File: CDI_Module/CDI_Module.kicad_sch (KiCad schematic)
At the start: 0 parts

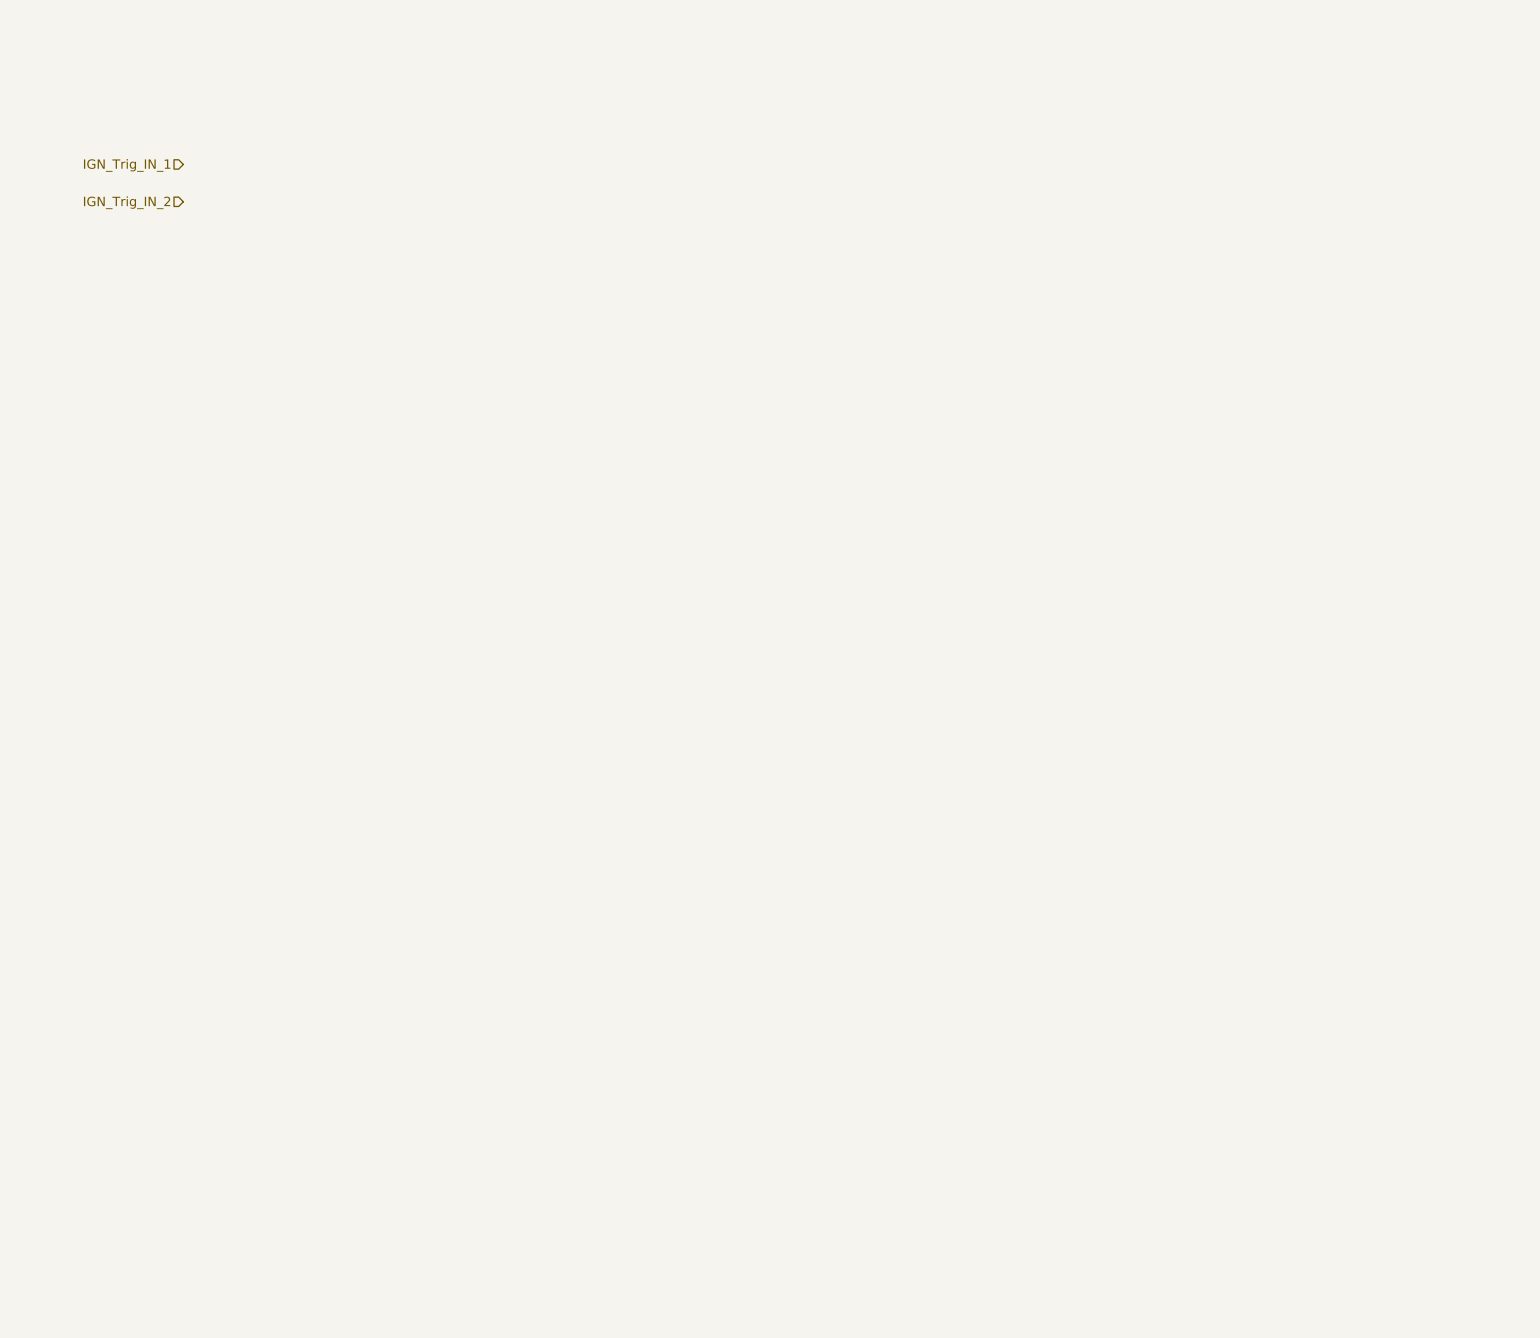
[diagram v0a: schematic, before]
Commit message: Updated security wiring and changed IGN driver for MOSFET
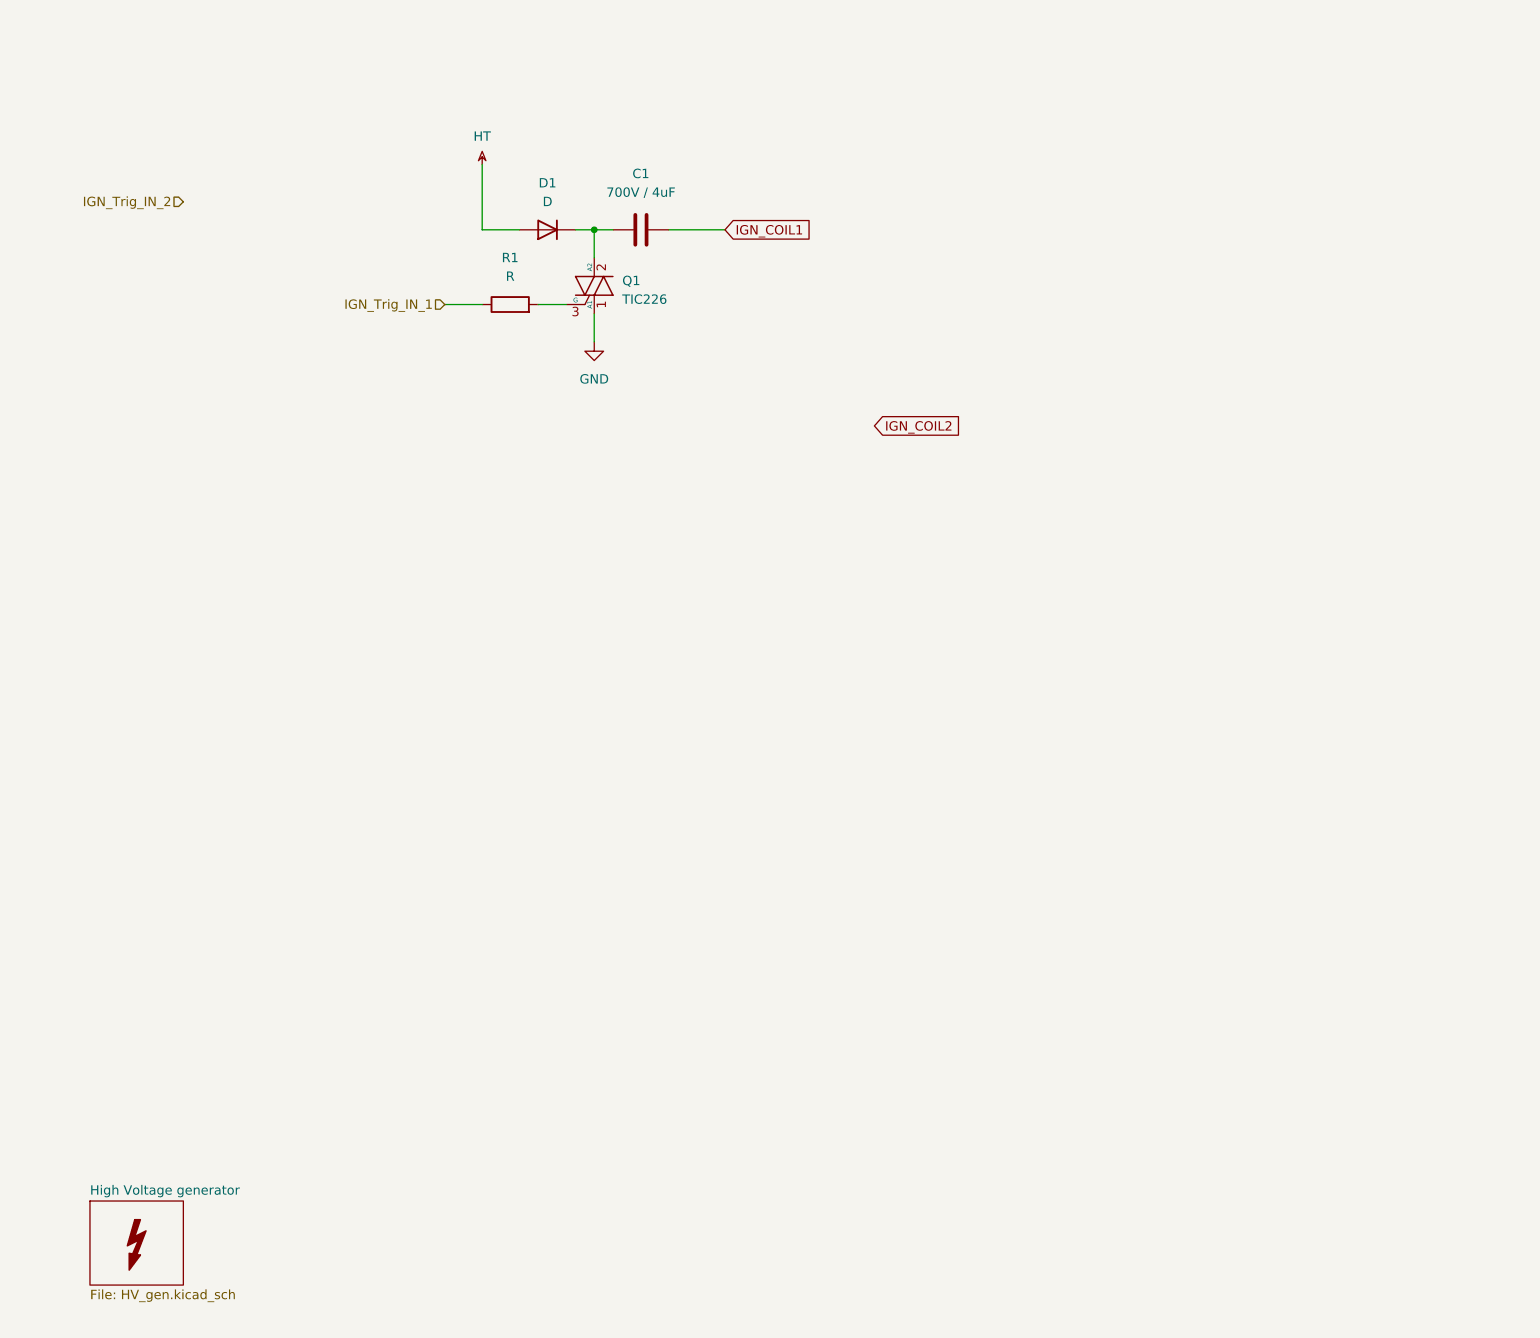
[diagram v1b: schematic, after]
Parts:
- added C1: 700V / 4uF, symbol Device:C
- added D1: D, Diode_SMD:D_0805_2012Metric_Pad1.15x1.40mm_HandSolder, symbol Device:D
- added Q1: TIC226, Package_TO_SOT_THT:TO-220-3_Vertical, symbol Triac_Thyristor:TIC226
- added R1: R, Resistor_SMD:R_0603_1608Metric_Pad0.98x0.95mm_HandSolder, symbol Device:R
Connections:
- net IGN_Trig_IN_1: now also R1.1
- new net: Q1.3 (G), R1.2
- new net: C1.1, D1.1 (K), Q1.2 (A2)
- new net GND: Q1.1 (A1)
- new net HT: D1.2 (A)
- new net IGN_COIL1: C1.2
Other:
- added sheet High Voltage generator (HV_gen.kicad_sch)
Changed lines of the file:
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@@
 (kicad_sch (version 20230121) (generator eeschema)
   (paper "A4")
-  (hierarchical_label "IGN_Trig_IN_1" (shape input) (at 43.18 36.83 180) (fields_autoplaced)
+  (junction (at 99.06 45.72) (diameter 0) (color 0 0 0 0)
+  )
+  (wire (pts (xy 96.52 45.72) (xy 99.06 45.72))
+    (stroke (width 0) (type default))
+  )
+  (wire (pts (xy 99.06 57.15) (xy 99.06 60.96))
+    (stroke (width 0) (type default))
+  )
+  (wire (pts (xy 88.9 45.72) (xy 83.82 45.72))
+    (stroke (width 0) (type default))
+  )
+  (wire (pts (xy 91.44 55.88) (xy 95.25 55.88))
+    (stroke (width 0) (type default))
+  )
+  (wire (pts (xy 109.22 45.72) (xy 116.84 45.72))
+    (stroke (width 0) (type default))
+  )
+  (wire (pts (xy 99.06 45.72) (xy 101.6 45.72))
+    (stroke (width 0) (type default))
+  )
+  (wire (pts (xy 83.82 45.72) (xy 83.82 36.83))
+    (stroke (width 0) (type default))
+  )
+  (wire (pts (xy 78.74 55.88) (xy 83.82 55.88))
+    (stroke (width 0) (type default))
+  )
+  (wire (pts (xy 99.06 49.53) (xy 99.06 45.72))
+    (stroke (width 0) (type default))
+  )
+  (global_label "IGN_COIL1" (shape input) (at 116.84 45.72 0) (fields_autoplaced)
+    (effects (font (size 1.27 1.27)) (justify left))
+    (property "Intersheetrefs" "${INTERSHEET_REFS}" (at 129.441 45.72 0)
+      (effects (font (size 1.27 1.27)) (justify left) hide)
+    )
+  )
+  (global_label "IGN_COIL2" (shape input) (at 137.16 72.39 0) (fields_autoplaced)
+    (effects (font (size 1.27 1.27)) (justify left))
+    (property "Intersheetrefs" "${INTERSHEET_REFS}" (at 149.761 72.39 0)
+      (effects (font (size 1.27 1.27)) (justify left) hide)
+    )
+  )
+  (hierarchical_label "IGN_Trig_IN_1" (shape input) (at 78.74 55.88 180) (fields_autoplaced)
     (effects (font (size 1.27 1.27)) (justify right))
   )
@@
     (effects (font (size 1.27 1.27)) (justify right))
   )
+  (symbol (lib_id "Device:R") (at 87.63 55.88 90) (unit 1)
+    (in_bom yes) (on_board yes) (dnp no) (fields_autoplaced)
+    (property "Reference" "R1" (at 87.63 49.53 90)
+      (effects (font (size 1.27 1.27)))
+    )
+    (property "Value" "R" (at 87.63 52.07 90)
+      (effects (font (size 1.27 1.27)))
+    )
+    (property "Footprint" "Resistor_SMD:R_0603_1608Metric_Pad0.98x0.95mm_HandSolder" (at 87.63 57.658 90)
+      (effects (font (size 1.27 1.27)) hide)
+    )
+    (property "Datasheet" "~" (at 87.63 55.88 0)
+      (effects (font (size 1.27 1.27)) hide)
+    )
+    (pin "1")
+    (pin "2")
+    (instances
+      (project "CDI_Module"
+        (path "/a4713233-3633-4d06-9186-8236551fb01a"
+          (reference "R1") (unit 1)
+        )
+      )
+    )
+  )
+  (symbol (lib_id "Triac_Thyristor:TIC226") (at 99.06 53.34 0) (unit 1)
+    (in_bom yes) (on_board yes) (dnp no) (fields_autoplaced)
+    (property "Reference" "Q1" (at 102.87 52.6542 0)
+      (effects (font (size 1.27 1.27)) (justify left))
+    )
+    (property "Value" "TIC226" (at 102.87 55.1942 0)
+      (effects (font (size 1.27 1.27)) (justify left))
+    )
+    (property "Footprint" "Package_TO_SOT_THT:TO-220-3_Vertical" (at 104.14 55.245 0)
+      (effects (font (size 1.27 1.27) italic) (justify left) hide)
+    )
+    (property "Datasheet" "http://pdf.datasheetcatalog.com/datasheet/PowerInnovations/mXuqxvy.pdf" (at 99.06 53.34 0)
+      (effects (font (size 1.27 1.27)) (justify left) hide)
+    )
+    (pin "3")
+    (pin "2")
+    (pin "1")
+    (instances
+      (project "CDI_Module"
+        (path "/a4713233-3633-4d06-9186-8236551fb01a"
+          (reference "Q1") (unit 1)
+        )
+      )
+    )
+  )
+  (symbol (lib_id "power:GND") (at 99.06 60.96 0) (unit 1)
+    (in_bom yes) (on_board yes) (dnp no) (fields_autoplaced)
+    (property "Reference" "#PWR02" (at 99.06 67.31 0)
+      (effects (font (size 1.27 1.27)) hide)
+    )
+    (property "Value" "GND" (at 99.06 66.04 0)
+      (effects (font (size 1.27 1.27)))
+    )
+    (property "Footprint" "" (at 99.06 60.96 0)
+      (effects (font (size 1.27 1.27)) hide)
+    )
+    (property "Datasheet" "" (at 99.06 60.96 0)
+      (effects (font (size 1.27 1.27)) hide)
+    )
+    (pin "1")
+    (instances
+      (project "CDI_Module"
+        (path "/a4713233-3633-4d06-9186-8236551fb01a"
+          (reference "#PWR02") (unit 1)
+        )
+      )
+    )
+  )
+  (symbol (lib_id "Device:C") (at 105.41 45.72 90) (unit 1)
+    (in_bom yes) (on_board yes) (dnp no) (fields_autoplaced)
+    (property "Reference" "C1" (at 105.41 38.1 90)
+      (effects (font (size 1.27 1.27)))
+    )
+    (property "Value" "700V / 4uF" (at 105.41 40.64 90)
+      (effects (font (size 1.27 1.27)))
+    )
+    (property "Footprint" "" (at 109.22 44.7548 0)
+      (effects (font (size 1.27 1.27)) hide)
+    )
+    (property "Datasheet" "~" (at 105.41 45.72 0)
+      (effects (font (size 1.27 1.27)) hide)
+    )
+    (pin "1")
+    (pin "2")
+    (instances
+      (project "CDI_Module"
+        (path "/a4713233-3633-4d06-9186-8236551fb01a"
+          (reference "C1") (unit 1)
+        )
+      )
+    )
+  )
+  (symbol (lib_id "power:HT") (at 83.82 36.83 0) (unit 1)
+    (in_bom yes) (on_board yes) (dnp no) (fields_autoplaced)
+    (property "Reference" "#PWR01" (at 83.82 33.782 0)
+      (effects (font (size 1.27 1.27)) hide)
+    )
+    (property "Value" "HT" (at 83.82 33.02 0)
+      (effects (font (size 1.27 1.27)))
+    )
+    (property "Footprint" "" (at 83.82 36.83 0)
+      (effects (font (size 1.27 1.27)) hide)
+    )
+    (property "Datasheet" "" (at 83.82 36.83 0)
+      (effects (font (size 1.27 1.27)) hide)
+    )
+    (pin "1")
+    (instances
+      (project "CDI_Module"
+        (path "/a4713233-3633-4d06-9186-8236551fb01a"
+          (reference "#PWR01") (unit 1)
+        )
+      )
+    )
+  )
+  (symbol (lib_id "Graphic:SYM_Flash_Small") (at 36.83 184.15 0) (unit 1)
+    (in_bom no) (on_board no) (dnp no) (fields_autoplaced)
+    (property "Reference" "#SYM1" (at 34.544 184.15 90)
+      (effects (font (size 1.27 1.27)) hide)
+    )
+    (property "Value" "SYM_Flash_Small" (at 39.116 184.15 90)
+      (effects (font (size 1.27 1.27)) hide)
+    )
+    (property "Footprint" "" (at 36.83 184.785 0)
+      (effects (font (size 1.27 1.27)) hide)
+    )
+    (property "Datasheet" "~" (at 46.99 186.69 0)
+      (effects (font (size 1.27 1.27)) hide)
+    )
+    (property "Sim.Enable" "0" (at 36.83 184.15 0)
+      (effects (font (size 1.27 1.27)) hide)
+    )
+    (instances
+      (project "CDI_Module"
+        (path "/a4713233-3633-4d06-9186-8236551fb01a"
+          (reference "#SYM1") (unit 1)
+        )
+      )
+    )
+  )
+  (symbol (lib_id "Device:D") (at 92.71 45.72 180) (unit 1)
+    (in_bom yes) (on_board yes) (dnp no) (fields_autoplaced)
+    (property "Reference" "D1" (at 92.71 39.37 0)
+      (effects (font (size 1.27 1.27)))
+    )
+    (property "Value" "D" (at 92.71 41.91 0)
+      (effects (font (size 1.27 1.27)))
+    )
+    (property "Footprint" "Diode_SMD:D_0805_2012Metric_Pad1.15x1.40mm_HandSolder" (at 92.71 45.72 0)
+      (effects (font (size 1.27 1.27)) hide)
+    )
+    (property "Datasheet" "~" (at 92.71 45.72 0)
+      (effects (font (size 1.27 1.27)) hide)
+    )
+    (property "Sim.Device" "D" (at 92.71 45.72 0)
+      (effects (font (size 1.27 1.27)) hide)
+    )
+    (property "Sim.Pins" "1=K 2=A" (at 92.71 45.72 0)
+      (effects (font (size 1.27 1.27)) hide)
+    )
+    (pin "1")
+    (pin "2")
+    (instances
+      (project "CDI_Module"
+        (path "/a4713233-3633-4d06-9186-8236551fb01a"
+          (reference "D1") (unit 1)
+        )
+      )
+    )
+  )
+  (sheet (at 30.48 177.8) (size 12.7 11.43) (fields_autoplaced)
+    (stroke (width 0.1524) (type solid))
+    (fill (color 0 0 0 0.0000))
+    (property "Sheetname" "High Voltage generator" (at 30.48 177.0884 0)
+      (effects (font (size 1.27 1.27)) (justify left bottom))
+    )
+    (property "Sheetfile" "HV_gen.kicad_sch" (at 30.48 189.8146 0)
+      (effects (font (size 1.27 1.27)) (justify left top))
+    )
+    (instances
+      (project "CDI_Module"
+        (path "/a4713233-3633-4d06-9186-8236551fb01a" (page "2"))
+      )
+    )
+  )
   (sheet_instances

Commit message: First Drawing of High volatage generator part
First Drawing of High volatage generator part
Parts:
- added R2: 10k, Resistor_SMD:R_0603_1608Metric_Pad0.98x0.95mm_HandSolder, symbol Device:R
- R1: value R -> 10k
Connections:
- net GND: now also R2.1
- net at Q1.3 (G), R1.2: now also R2.2
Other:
- moved on the sheet: R1
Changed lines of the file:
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@@
 (kicad_sch (version 20230121) (generator eeschema)
   (paper "A4")
+  (junction (at 91.44 55.88) (diameter 0) (color 0 0 0 0)
+  )
   (junction (at 99.06 45.72) (diameter 0) (color 0 0 0 0)
   )
+  (junction (at 99.06 67.31) (diameter 0) (color 0 0 0 0)
+  )
+  (wire (pts (xy 99.06 67.31) (xy 99.06 68.58))
+    (stroke (width 0) (type default))
+  )
+  (wire (pts (xy 91.44 55.88) (xy 91.44 58.42))
+    (stroke (width 0) (type default))
+  )
   (wire (pts (xy 96.52 45.72) (xy 99.06 45.72))
     (stroke (width 0) (type default))
   )
-  (wire (pts (xy 99.06 57.15) (xy 99.06 60.96))
+  (wire (pts (xy 99.06 57.15) (xy 99.06 67.31))
     (stroke (width 0) (type default))
   )
@@
     (stroke (width 0) (type default))
   )
+  (wire (pts (xy 88.9 55.88) (xy 91.44 55.88))
+    (stroke (width 0) (type default))
+  )
+  (wire (pts (xy 109.22 45.72) (xy 116.84 45.72))
+    (stroke (width 0) (type default))
+  )
   (wire (pts (xy 91.44 55.88) (xy 95.25 55.88))
     (stroke (width 0) (type default))
   )
-  (wire (pts (xy 109.22 45.72) (xy 116.84 45.72))
+  (wire (pts (xy 91.44 67.31) (xy 91.44 66.04))
     (stroke (width 0) (type default))
   )
@@
     (stroke (width 0) (type default))
   )
-  (wire (pts (xy 78.74 55.88) (xy 83.82 55.88))
+  (wire (pts (xy 78.74 55.88) (xy 81.28 55.88))
     (stroke (width 0) (type default))
   )
   (wire (pts (xy 99.06 49.53) (xy 99.06 45.72))
+    (stroke (width 0) (type default))
+  )
+  (wire (pts (xy 91.44 67.31) (xy 99.06 67.31))
     (stroke (width 0) (type default))
   )
@@
     (effects (font (size 1.27 1.27)) (justify right))
   )
-  (symbol (lib_id "Device:R") (at 87.63 55.88 90) (unit 1)
-    (in_bom yes) (on_board yes) (dnp no) (fields_autoplaced)
-    (property "Reference" "R1" (at 87.63 49.53 90)
-      (effects (font (size 1.27 1.27)))
-    )
-    (property "Value" "R" (at 87.63 52.07 90)
-      (effects (font (size 1.27 1.27)))
-    )
-    (property "Footprint" "Resistor_SMD:R_0603_1608Metric_Pad0.98x0.95mm_HandSolder" (at 87.63 57.658 90)
-      (effects (font (size 1.27 1.27)) hide)
-    )
-    (property "Datasheet" "~" (at 87.63 55.88 0)
+  (symbol (lib_id "Device:R") (at 85.09 55.88 90) (unit 1)
+    (in_bom yes) (on_board yes) (dnp no) (fields_autoplaced)
+    (property "Reference" "R1" (at 85.09 49.53 90)
+      (effects (font (size 1.27 1.27)))
+    )
+    (property "Value" "10k" (at 85.09 52.07 90)
+      (effects (font (size 1.27 1.27)))
+    )
+    (property "Footprint" "Resistor_SMD:R_0603_1608Metric_Pad0.98x0.95mm_HandSolder" (at 85.09 57.658 90)
+      (effects (font (size 1.27 1.27)) hide)
+    )
+    (property "Datasheet" "~" (at 85.09 55.88 0)
       (effects (font (size 1.27 1.27)) hide)
     )
@@
     )
   )
-  (symbol (lib_id "power:GND") (at 99.06 60.96 0) (unit 1)
-    (in_bom yes) (on_board yes) (dnp no) (fields_autoplaced)
-    (property "Reference" "#PWR02" (at 99.06 67.31 0)
-      (effects (font (size 1.27 1.27)) hide)
-    )
-    (property "Value" "GND" (at 99.06 66.04 0)
-      (effects (font (size 1.27 1.27)))
-    )
-    (property "Footprint" "" (at 99.06 60.96 0)
-      (effects (font (size 1.27 1.27)) hide)
-    )
-    (property "Datasheet" "" (at 99.06 60.96 0)
+  (symbol (lib_id "power:GND") (at 99.06 68.58 0) (unit 1)
+    (in_bom yes) (on_board yes) (dnp no) (fields_autoplaced)
+    (property "Reference" "#PWR02" (at 99.06 74.93 0)
+      (effects (font (size 1.27 1.27)) hide)
+    )
+    (property "Value" "GND" (at 99.06 73.66 0)
+      (effects (font (size 1.27 1.27)))
+    )
+    (property "Footprint" "" (at 99.06 68.58 0)
+      (effects (font (size 1.27 1.27)) hide)
+    )
+    (property "Datasheet" "" (at 99.06 68.58 0)
       (effects (font (size 1.27 1.27)) hide)
     )
@@
         )
       )
+    )
+  )
+  (symbol (lib_id "Device:R") (at 91.44 62.23 180) (unit 1)
+    (in_bom yes) (on_board yes) (dnp no) (fields_autoplaced)
+    (property "Reference" "R2" (at 93.98 60.96 0)
+      (effects (font (size 1.27 1.27)) (justify right))
+    )
+    (property "Value" "10k" (at 93.98 63.5 0)
+      (effects (font (size 1.27 1.27)) (justify right))
+    )
+    (property "Footprint" "Resistor_SMD:R_0603_1608Metric_Pad0.98x0.95mm_HandSolder" (at 93.218 62.23 90)
+      (effects (font (size 1.27 1.27)) hide)
+    )
+    (property "Datasheet" "~" (at 91.44 62.23 0)
+      (effects (font (size 1.27 1.27)) hide)
+    )
+    (pin "1")
+    (pin "2")
+    (instances
+      (project "CDI_Module"
+        (path "/a4713233-3633-4d06-9186-8236551fb01a"
+          (reference "R2") (unit 1)
+        )
+      )
